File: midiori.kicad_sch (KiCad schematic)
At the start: 94 parts, among them J1 midiori-rescue_x68000_expansi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, J2 Conn_ARM_JTAG_SWD_10, J3 AudioJack3, J4 Mini-DIN-5, J5 AudioJack3, J6 AudioJack3, J7 Conn_01x06, J8 AudioJack3, J9 Mini-DIN-5, U1 74lv07, U10 ICE40HX1K-TQ144, U11 AP2205K-3.3, U12 AK4432, U13 TL072, U14 AP2205K-3.3, U15 TL072, U16 74lv07, U17 H11L1, U18 SN74LVC245APW, U19 74lv07, U2 AT25SF081-SSHD-X, U3 AP2127K-1.2, U4 SN74LVC245APW, U5 SN74LVC245APW, U6 SN74LVC245APW, U7 SN74LVC245APW, U8 SN74LVC245APW, U9 SN74LVC245APW, X1 16MHz, X2 24.576MHz

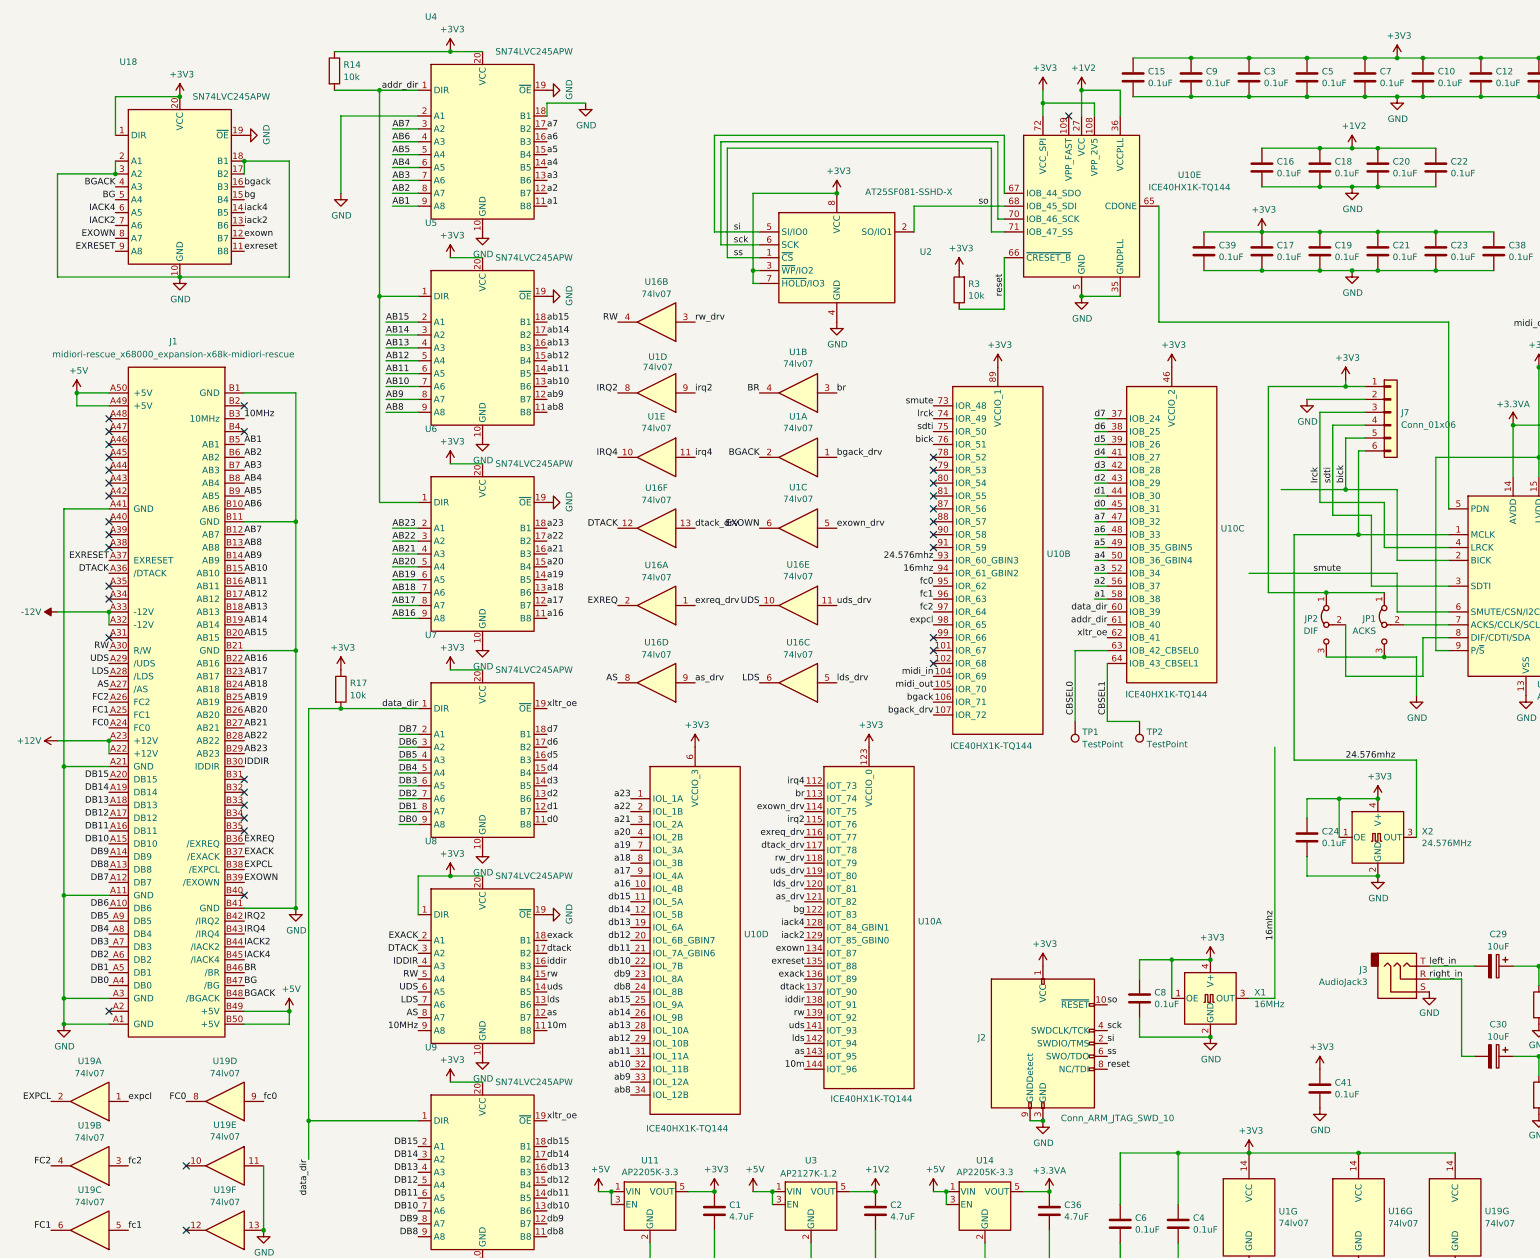
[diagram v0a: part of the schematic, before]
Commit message: Swap to hx4k and add 20mhz
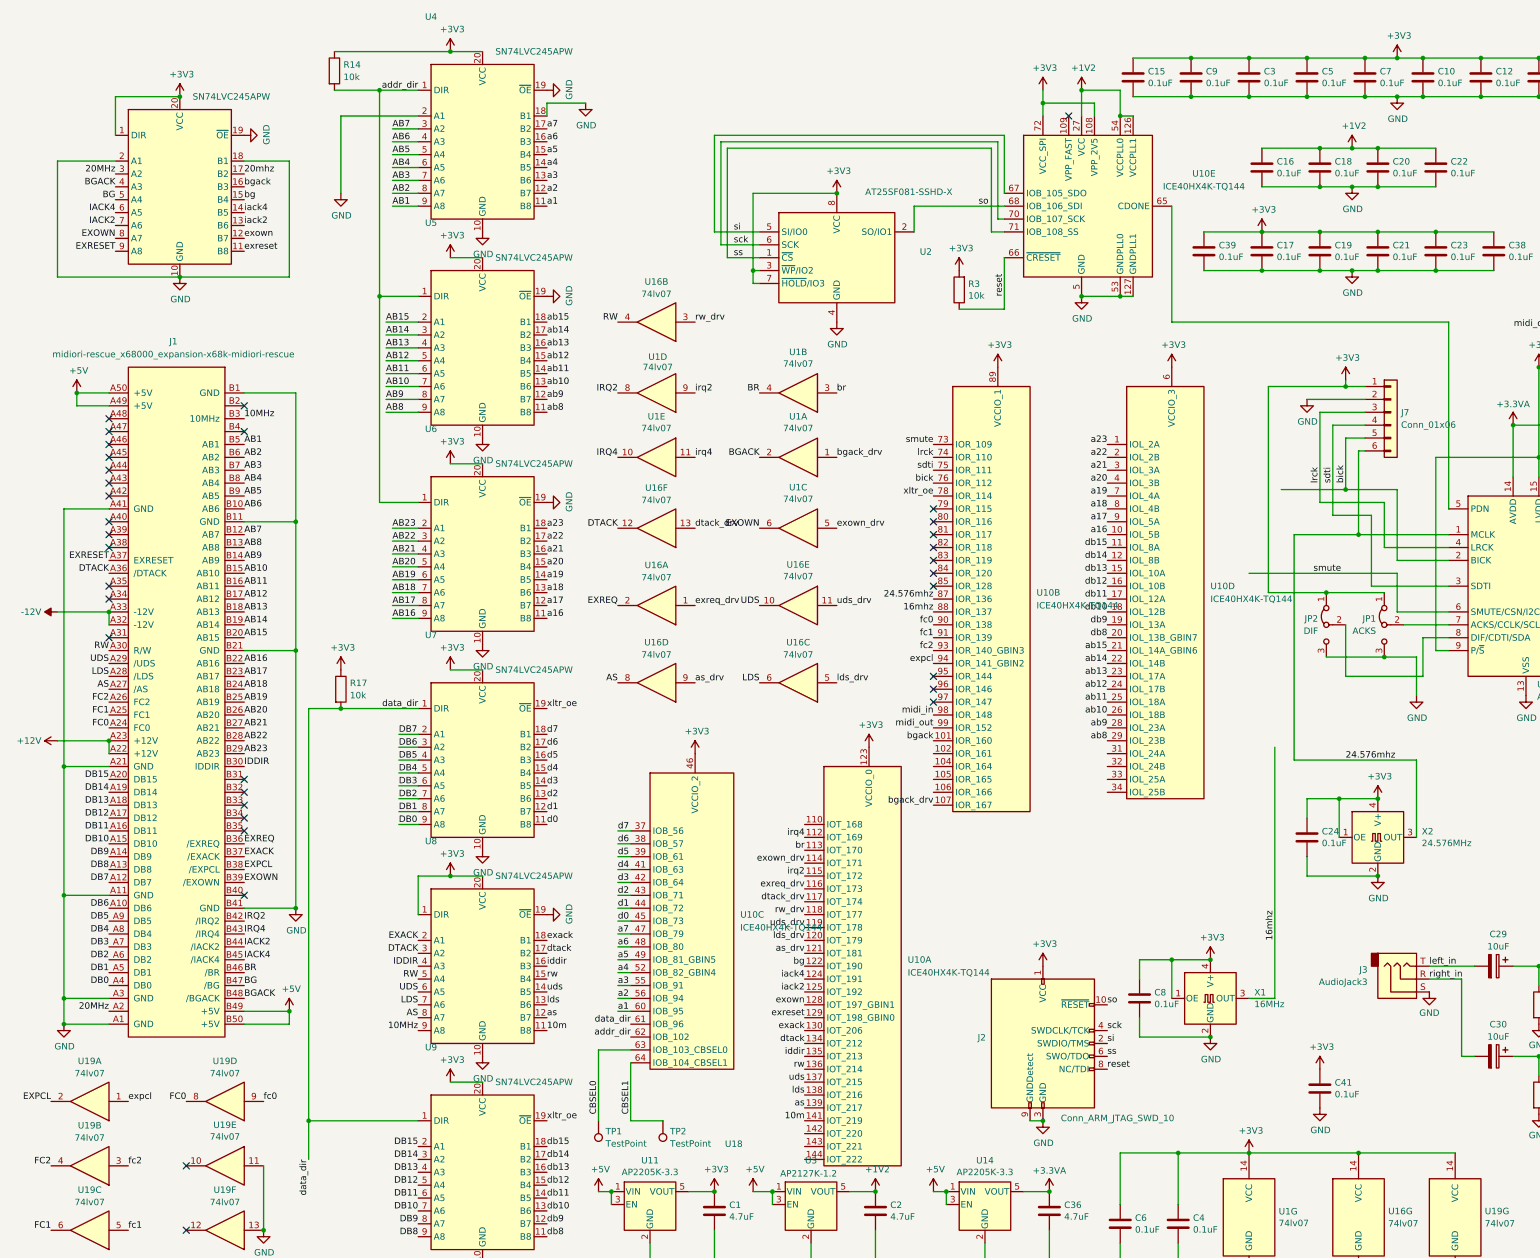
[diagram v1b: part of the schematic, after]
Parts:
- removed U10: ICE40HX1K-TQ144, Package_QFP:TQFP-144_20x20mm_P0.5mm, symbol FPGA_Lattice:ICE40HX1K-TQ144
- added U10: ICE40HX4K-TQ144, Package_QFP:TQFP-144_20x20mm_P0.5mm, symbol FPGA_Lattice:ICE40HX4K-TQ144
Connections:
- net +1V2: now also U10.111 (VCC), U10.126 (VCCPLL1), U10.27 (VCC), U10.40 (VCC), U10.54 (VCCPLL0), U10.92 (VCC)
- net +3V3: now also U10.100 (VCCIO_1), U10.108 (VPP_2V5), U10.123 (VCCIO_0), U10.131 (VCCIO_0), U10.30 (VCCIO_3), U10.46 (VCCIO_2), U10.57 (VCCIO_2), U10.6 (VCCIO_3), U10.72 (VCC_SPI), U10.89 (VCCIO_1)
- net 10m: now also U10.141 (IOT_219)
- net 16mhz: now also U10.88 (IOR_137)
- net 24.576mhz: now also U10.87 (IOR_136)
- net CBSEL0: now also U10.63 (IOB_103_CBSEL0)
- net CBSEL1: now also U10.64 (IOB_104_CBSEL1)
- net GND: now also U10.103 (GND), U10.127 (GNDPLL1), U10.13 (GND), U10.132 (GND), U10.14 (GND), U10.140 (GND), U10.5 (GND), U10.53 (GNDPLL0), U10.59 (GND), U10.69 (GND), U10.86 (GND); no longer U18.17 (B2), U18.3 (A2)
- net a1: now also U10.60 (IOB_95)
- net a16: now also U10.10 (IOL_5B)
- net a17: now also U10.9 (IOL_5A)
- net a18: now also U10.8 (IOL_4B)
- net a19: now also U10.7 (IOL_4A)
- net a2: now also U10.56 (IOB_94)
- net a20: now also U10.4 (IOL_3B)
- net a21: now also U10.3 (IOL_3A)
- net a22: now also U10.2 (IOL_2B)
- net a23: now also U10.1 (IOL_2A)
- net a3: now also U10.55 (IOB_91)
- net a4: now also U10.52 (IOB_82_GBIN4)
- net a5: now also U10.49 (IOB_81_GBIN5)
- net a6: now also U10.48 (IOB_80)
- net a7: now also U10.47 (IOB_79)
- net ab10: now also U10.26 (IOL_18B)
- net ab11: now also U10.25 (IOL_18A)
- net ab12: now also U10.24 (IOL_17B)
- net ab13: now also U10.23 (IOL_17A)
- net ab14: now also U10.22 (IOL_14B)
- net ab15: now also U10.21 (IOL_14A_GBIN6)
- net ab8: now also U10.29 (IOL_23B)
- net ab9: now also U10.28 (IOL_23A)
- net addr_dir: now also U10.62 (IOB_102)
- net as: now also U10.139 (IOT_217)
- net as_drv: now also U10.121 (IOT_181)
- net bg: now also U10.122 (IOT_190)
- net bgack: now also U10.101 (IOR_160)
- net bgack_drv: now also U10.107 (IOR_167)
- net bick: now also U10.76 (IOR_112)
- net br: now also U10.113 (IOT_170)
- net d0: now also U10.45 (IOB_73)
- net d1: now also U10.44 (IOB_72)
- net d2: now also U10.43 (IOB_71)
- net d3: now also U10.42 (IOB_64)
- net d4: now also U10.41 (IOB_63)
- net d5: now also U10.39 (IOB_61)
- net d6: now also U10.38 (IOB_57)
- net d7: now also U10.37 (IOB_56)
- net data_dir: now also U10.61 (IOB_96)
- net db10: now also U10.18 (IOL_12B)
- net db11: now also U10.17 (IOL_12A)
- net db12: now also U10.16 (IOL_10B)
- net db13: now also U10.15 (IOL_10A)
- net db14: now also U10.12 (IOL_8B)
- net db15: now also U10.11 (IOL_8A)
- net db8: now also U10.20 (IOL_13B_GBIN7)
- net db9: now also U10.19 (IOL_13A)
- net dtack: now also U10.134 (IOT_212)
- net dtack_drv: now also U10.117 (IOT_174)
- net exack: now also U10.130 (IOT_206)
- net exown: now also U10.128 (IOT_197_GBIN1)
- net exown_drv: now also U10.114 (IOT_171)
- net expcl: now also U10.94 (IOR_141_GBIN2)
- net exreq_drv: now also U10.116 (IOT_173)
- net exreset: now also U10.129 (IOT_198_GBIN0)
- net fc0: now also U10.90 (IOR_138)
- net fc1: now also U10.91 (IOR_139)
- net fc2: now also U10.93 (IOR_140_GBIN3)
- net iack2: now also U10.125 (IOT_192)
- net iack4: now also U10.124 (IOT_191)
- net iddir: now also U10.135 (IOT_213)
- net irq2: now also U10.115 (IOT_172)
- net irq4: now also U10.112 (IOT_169)
- net lds: now also U10.138 (IOT_216)
- net lds_drv: now also U10.120 (IOT_179)
- net lrck: now also U10.74 (IOR_110)
- net midi_in: now also U10.98 (IOR_148)
- net midi_out: now also U10.99 (IOR_152)
- net reset: now also U10.66 (~{CRESET})
- net rw: now also U10.136 (IOT_214)
- net rw_drv: now also U10.118 (IOT_177)
- net sck: now also U10.70 (IOB_107_SCK)
- net sdti: now also U10.75 (IOR_111)
- net si: now also U10.67 (IOB_105_SDO)
- net smute: now also U10.73 (IOR_109)
- net so: now also U10.68 (IOB_106_SDI)
- net ss: now also U10.71 (IOB_108_SS)
- net uds: now also U10.137 (IOT_215)
- net uds_drv: now also U10.119 (IOT_178)
- net xltr_oe: now also U10.78 (IOR_114)
- net 20MHz: now reaches J1.A2
- net 20MHz: now also U18.3 (A2)
- net at U12.5 (PDN): now also U10.65 (CDONE)
- new net 20mhz: U18.17 (B2)
- no-connect marks 42 -> 40
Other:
- moved on the sheet: TP1, TP2
